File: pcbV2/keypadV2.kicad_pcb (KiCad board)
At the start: 2 copper layers, 93.7 x 93.3 mm, 59 parts, among them J1 Conn_01x02_Female, J2 USB_C_Receptacle, J3 Conn_01x03_Male, J6 Conn_01x03_Male, Q1 Q_NMOS_GSD, Q2 Q_NMOS_GSD, SW1 SW_Push, SW10 SW_Push, SW11 SW_Push, SW12 SW_Push, SW13 SW_SPDT, SW14 SW_Push, SW15 SW_Push, SW16 SW_Push, SW17 SW_DIP_x03, SW2 SW_Push, SW3 SW_Push, SW4 SW_Push, SW5 SW_Push, SW6 SW_Push, SW7 SW_Push, SW8 SW_Push, SW9 SW_Push, U1 Teensy4.0, U2 Waveshare_OLED_RGB

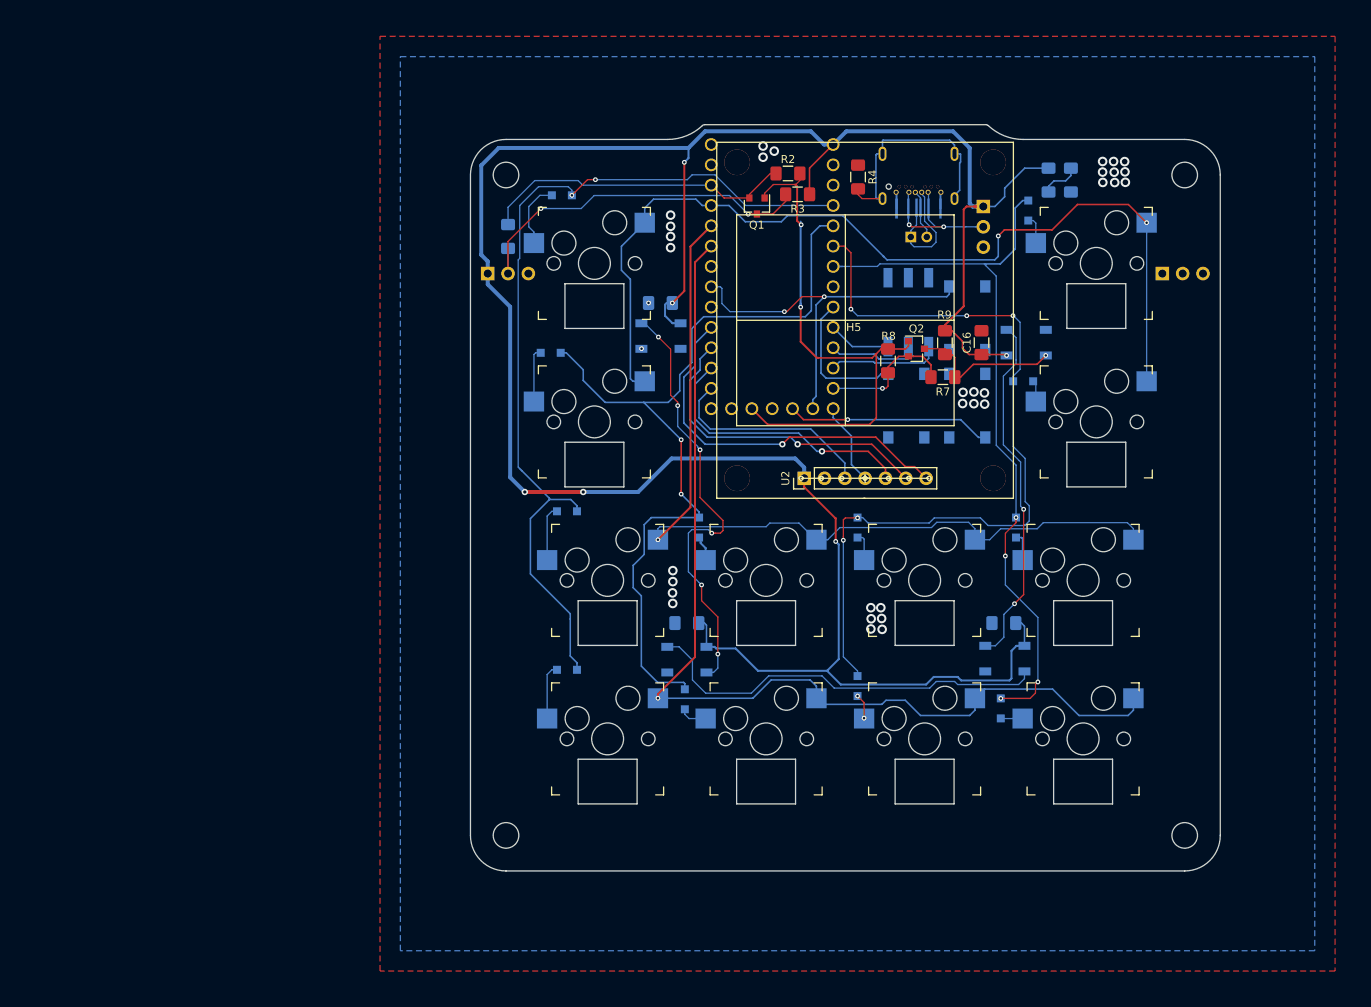
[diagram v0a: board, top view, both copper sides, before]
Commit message: removed usb c
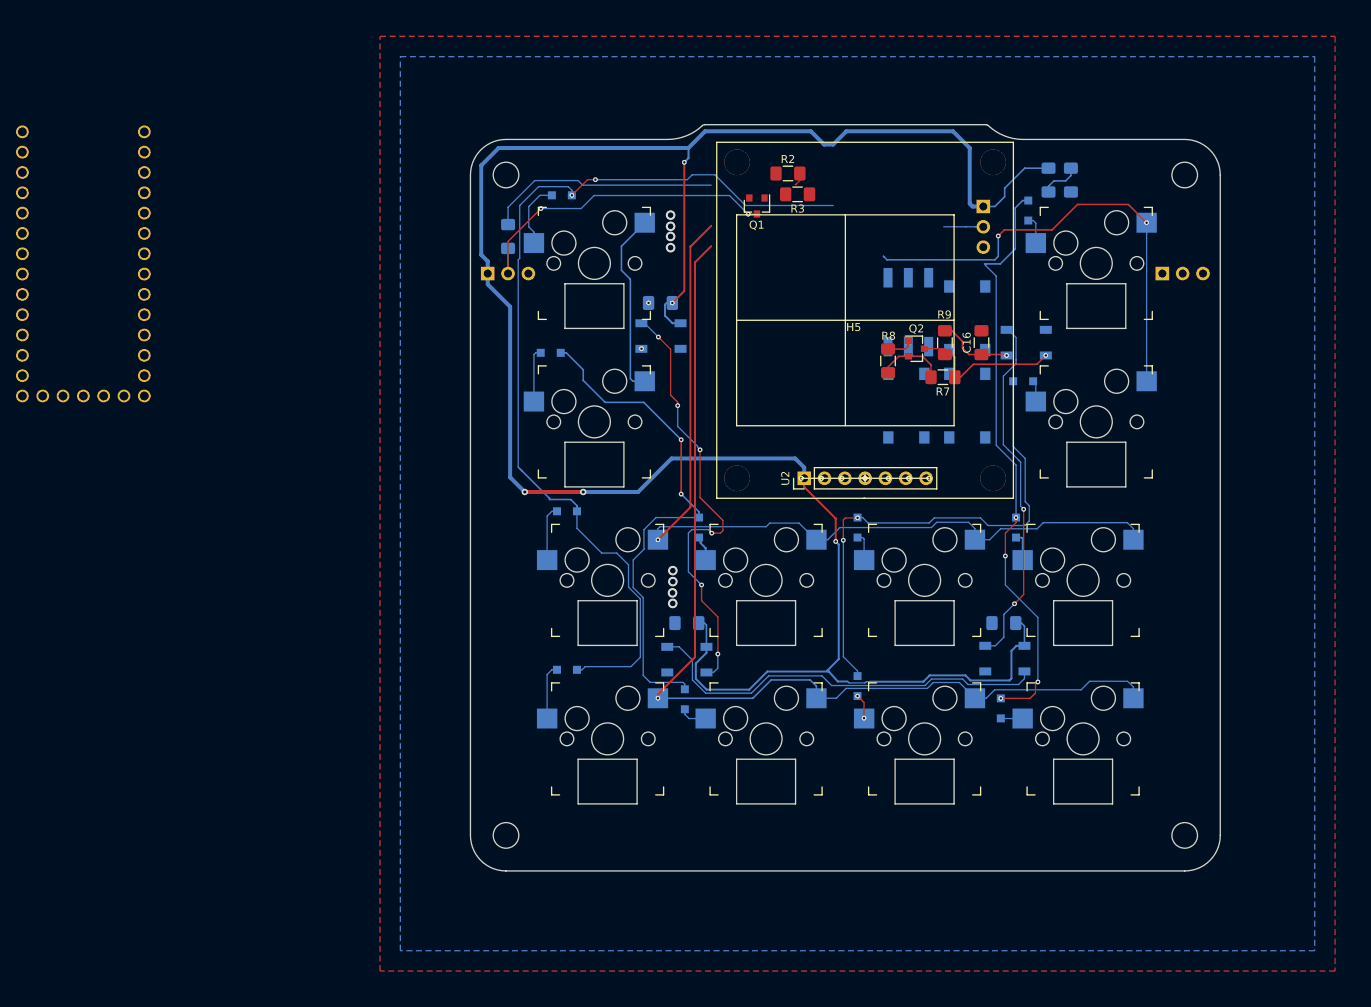
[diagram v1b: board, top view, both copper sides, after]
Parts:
- removed J1: Conn_01x02_Female, Connector_PinHeader_2.00mm:PinHeader_1x02_P2.00mm_Vertical
- removed J2: USB_C_Receptacle, custom:USB_C_REDUCED_UJ31-CH-G2
- removed R4: R_SHIELD, Resistor_SMD:R_1206_3216Metric_Pad1.42x1.75mm_HandSolder
- moved U1 86.1 mm to (86.6, 61.0)
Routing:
- net +3V3: track 67.6 -> 4.99 mm, vias 2 -> 0
- net ON_OFF: track 48.6 -> 0.00 mm, vias 2 -> 0
- net DISP_RST: track 47.3 -> 0.00 mm, vias 1 -> 0
- net COL2: track 106.0 -> 64.1 mm
- net DISP_DC: track 40.1 -> 0.00 mm, vias 1 -> 0
- net COL3: track 102.2 -> 63.1 mm, vias 5 -> 2
- net ROW1: track 117.1 -> 81.4 mm
- net CS: track 34.8 -> 0.00 mm, vias 1 -> 0
- net Net-(J2-PadS1): track 29.7 -> 0.00 mm
- net MOSI: track 26.8 -> 0.00 mm
- net PRGM: track 25.6 -> 0.00 mm, vias 1 -> 0
- net +5V: track 306.9 -> 287.0 mm
- net COL4: track 93.0 -> 74.0 mm
- net BTN: track 17.8 -> 0.00 mm
- net USB_DATA+: track 15.6 -> 0.00 mm
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
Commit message: started rewiring
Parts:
- removed SW13: SW_SPDT, Connector_PinHeader_2.54mm:PinHeader_1x03_P2.54mm_Vertical
- C16: moved to B.Cu
- moved U1 95.3 mm to (181.9, 62.7)
- moved SW14 29.3 mm to (168.1, 63.0), turned to 180 degrees
- moved SW15 29.2 mm to (168.1, 75.2)
- moved Q1 11.6 mm to (182.4, 53.6)
- moved SW17 10.0 mm to (197.4, 60.5)
- moved SW16 9.06 mm to (196.8, 73.4)
- moved R9 8.58 mm to (185.9, 69.0)
- moved C16 7.63 mm to (203.7, 64.9)
- moved R2 7.56 mm to (182.2, 49.4)
- moved Q2 5.26 mm to (185.9, 73.7), turned to 90 degrees
- moved R8 3.84 mm to (185.9, 76.7), turned to 0 degrees
- moved R7 2.73 mm to (196.7, 74.5)
- moved R3 2.48 mm to (178.2, 53.2), turned to 270 degrees
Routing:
- net COL4: track 74.0 -> 28.9 mm
- net COL2: track 64.1 -> 109.1 mm, vias 2 -> 0
- net ROW1: track 81.4 -> 41.4 mm, vias 2 -> 0
- net DISP_RST: track 0.00 -> 32.0 mm
- net COL3: track 63.1 -> 91.1 mm
- net DISP_DC: track 0.00 -> 26.7 mm
- net +5V: track 287.0 -> 261.6 mm
- net SCK: track 0.00 -> 22.2 mm
- net CS: track 0.00 -> 21.9 mm
- net RGB_DATA1: track 29.2 -> 49.2 mm
- net Net-(D26-Pad4): track 55.2 -> 36.1 mm, vias 6 -> 3
- net RGB_UNDER: track 19.6 -> 1.57 mm, vias 1 -> 0
- net DIP1: track 0.00 -> 17.6 mm
- net MOSI: track 0.00 -> 17.0 mm
- net DIP2: track 0.00 -> 12.9 mm
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- removed copper zone on B.Cu, net GND

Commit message: v2 layout
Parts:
- C16: moved to F.Cu
- moved C16 5.88 mm to (204.3, 70.7)
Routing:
- net ROW1: track 41.4 -> 112.0 mm
- net +5V: track 261.6 -> 322.4 mm, vias 6 -> 7
- net COL4: track 28.9 -> 71.9 mm, vias 4 -> 5
- net +3V3: track 3.36 -> 43.7 mm, vias 0 -> 2
- net ON_OFF: track 5.07 -> 34.4 mm, vias 0 -> 1
- net RGB_UNDER: track 1.57 -> 27.1 mm
- net COL2: track 109.1 -> 134.3 mm, vias 0 -> 2
- net PRGM: track 0.00 -> 15.8 mm, vias 0 -> 1
- net Net-(D26-Pad4): track 36.1 -> 48.9 mm, vias 3 -> 2
- net RGB_DATA2: track 0.00 -> 11.5 mm
- net BTN: track 0.00 -> 7.16 mm, vias 0 -> 1
- net ROW2: track 113.5 -> 120.2 mm
- net ROW3: track 137.7 -> 140.0 mm
- net COL1: track 128.8 -> 127.4 mm
- net RGB_DIN: track 54.2 -> 55.0 mm, vias 2 -> 3
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- added copper zone on B.Cu, net GND

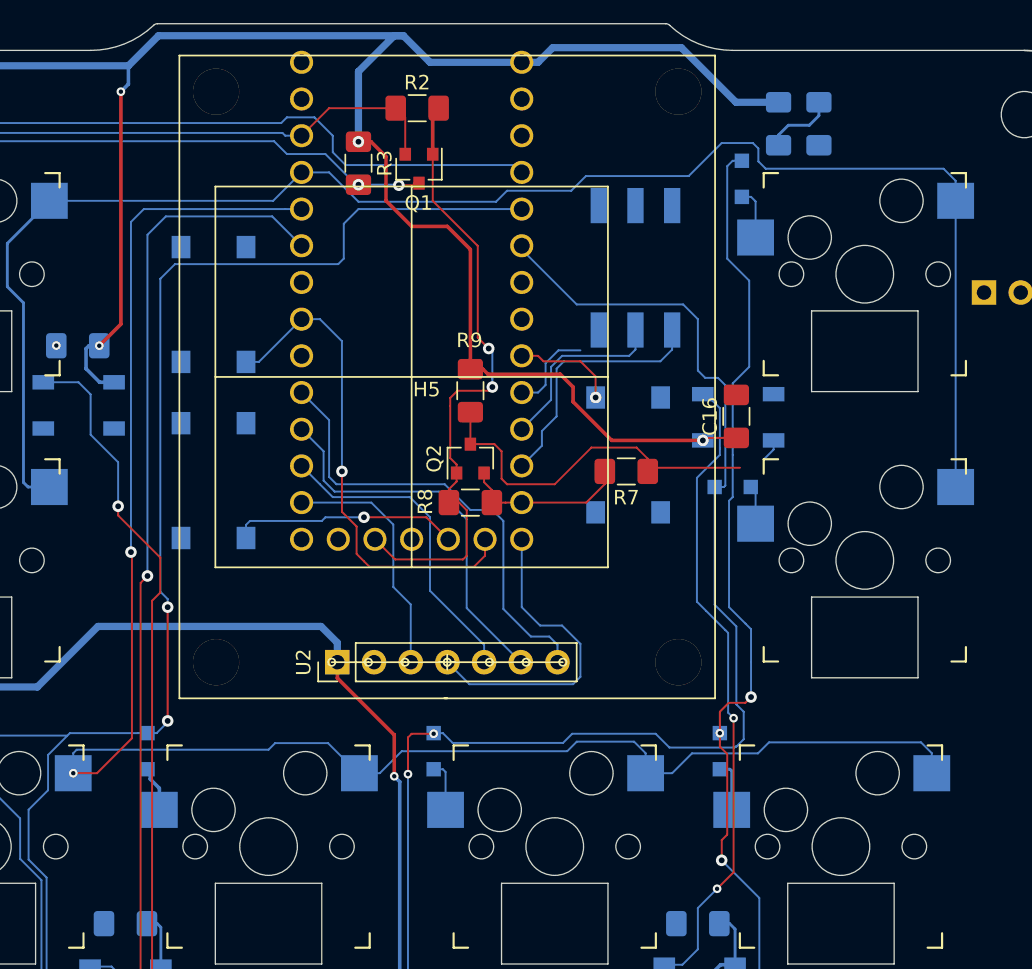
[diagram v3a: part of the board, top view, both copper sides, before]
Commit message: edited layout, updated daughter board
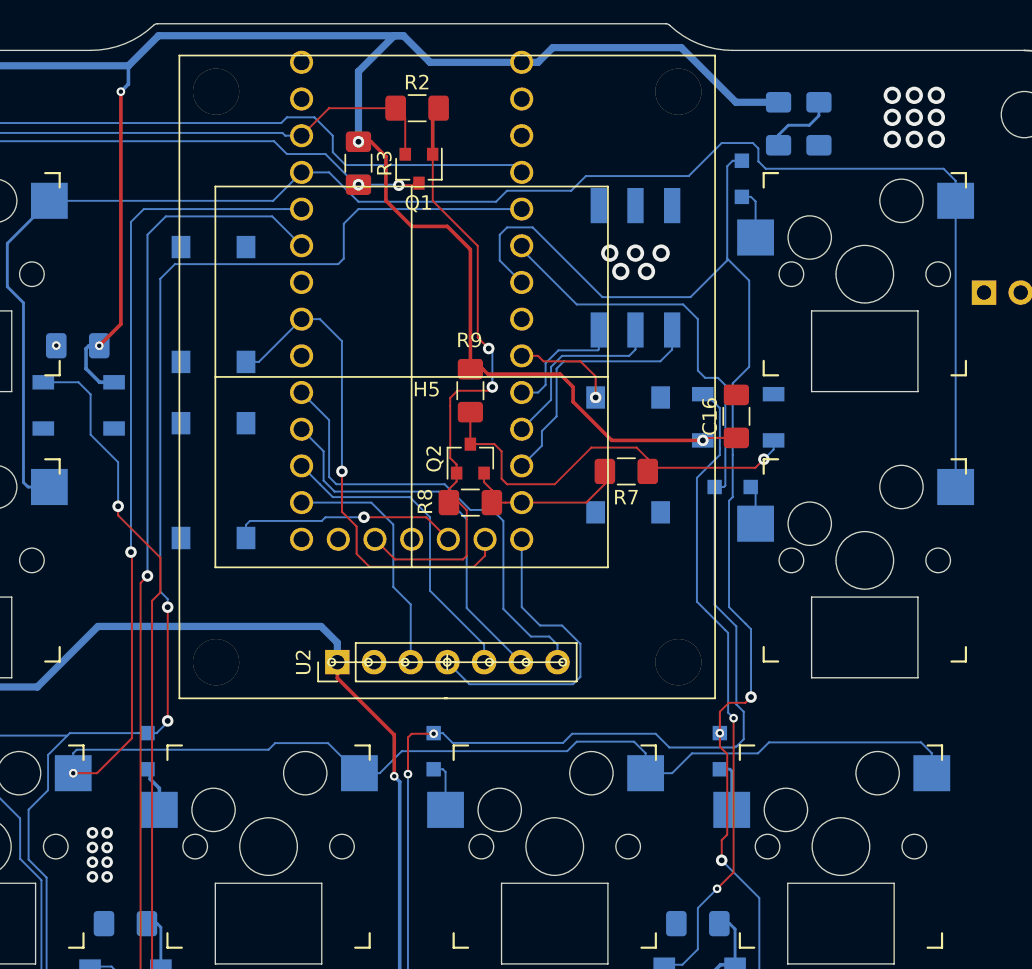
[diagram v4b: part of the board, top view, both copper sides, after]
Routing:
- net COL4: track 71.9 -> 95.0 mm
- net DIP3: track 6.16 -> 8.81 mm
- net RGB_UNDER: track 27.1 -> 29.0 mm, vias 0 -> 1
- net GND: vias 1 -> 23
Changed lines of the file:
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@@
     (thickness 1.6)
     (drawings 64)
-    (tracks 594)
+    (tracks 628)
     (zones 0)
     (modules 55)
@@
   (gr_arc (start 139.446 132.3975) (end 135.001 132.3975) (angle -90) (layer Edge.Cuts) (width 0.12))
   (via (at 157.2641 65.8368) (size 0.6) (drill 0.3) (layers F.Cu B.Cu) (net 1))
+  (via (at 215.138 48.514) (size 1.2) (drill 0.7) (layers F.Cu B.Cu) (net 1))
+  (via (at 216.662 48.514) (size 1.2) (drill 0.7) (layers F.Cu B.Cu) (net 1))
+  (via (at 215.138 50.038) (size 1.2) (drill 0.7) (layers F.Cu B.Cu) (net 1))
+  (via (at 216.662 50.038) (size 1.2) (drill 0.7) (layers F.Cu B.Cu) (net 1))
+  (via (at 218.186 50.038) (size 1.2) (drill 0.7) (layers F.Cu B.Cu) (net 1))
+  (via (at 218.186 48.514) (size 1.2) (drill 0.7) (layers F.Cu B.Cu) (net 1))
+  (via (at 218.186 51.562) (size 1.2) (drill 0.7) (layers F.Cu B.Cu) (net 1))
+  (via (at 216.662 51.562) (size 1.2) (drill 0.7) (layers F.Cu B.Cu) (net 1))
+  (via (at 215.138 51.562) (size 1.2) (drill 0.7) (layers F.Cu B.Cu) (net 1))
+  (via (at 195.58 59.436) (size 1.2) (drill 0.7) (layers F.Cu B.Cu) (net 1))
+  (via (at 197.358 59.436) (size 1.2) (drill 0.7) (layers F.Cu B.Cu) (net 1))
+  (via (at 199.136 59.436) (size 1.2) (drill 0.7) (layers F.Cu B.Cu) (net 1))
+  (via (at 198.12 60.706) (size 1.2) (drill 0.7) (layers F.Cu B.Cu) (net 1))
+  (via (at 196.342 60.706) (size 1.2) (drill 0.7) (layers F.Cu B.Cu) (net 1))
+  (via (at 160.782 100.584) (size 0.8) (drill 0.4) (layers F.Cu B.Cu) (net 1))
+  (via (at 160.782 101.6) (size 0.8) (drill 0.4) (layers F.Cu B.Cu) (net 1))
+  (via (at 160.782 102.616) (size 0.8) (drill 0.4) (layers F.Cu B.Cu) (net 1))
+  (via (at 159.766 102.616) (size 0.8) (drill 0.4) (layers F.Cu B.Cu) (net 1))
+  (via (at 159.766 101.6) (size 0.8) (drill 0.4) (layers F.Cu B.Cu) (net 1))
+  (via (at 159.766 100.584) (size 0.8) (drill 0.4) (layers F.Cu B.Cu) (net 1))
+  (via (at 160.782 99.568) (size 0.8) (drill 0.4) (layers F.Cu B.Cu) (net 1))
+  (via (at 159.766 99.568) (size 0.8) (drill 0.4) (layers F.Cu B.Cu) (net 1))
   (segment (start 162.2552 46.4693) (end 138.5316 46.4693) (width 0.5) (layer B.Cu) (net 2))
   (segment (start 138.5316 46.4693) (end 136.3472 48.6537) (width 0.5) (layer B.Cu) (net 2))
@@
   (segment (start 205.359 90.17) (end 205.359 90.17) (width 0.135) (layer B.Cu) (net 10))
   (via (at 205.359 90.17) (size 0.8) (drill 0.4) (layers F.Cu B.Cu) (net 10))
+  (segment (start 189.484 61.468) (end 187.96 59.944) (width 0.135) (layer B.Cu) (net 10))
+  (segment (start 187.96 59.944) (end 187.96 58.166) (width 0.135) (layer B.Cu) (net 10))
+  (segment (start 187.96 58.166) (end 188.468 57.658) (width 0.135) (layer B.Cu) (net 10))
+  (segment (start 188.468 57.658) (end 190.246 57.658) (width 0.135) (layer B.Cu) (net 10))
+  (segment (start 190.246 57.658) (end 195.072 62.484) (width 0.135) (layer B.Cu) (net 10))
+  (segment (start 195.072 62.484) (end 201.168 62.484) (width 0.135) (layer B.Cu) (net 10))
+  (segment (start 201.168 62.484) (end 203.708 59.944) (width 0.135) (layer B.Cu) (net 10))
+  (segment (start 203.708 59.944) (end 203.708 59.817) (width 0.135) (layer B.Cu) (net 10))
   (segment (start 145.181 91.8845) (end 145.816 91.8845) (width 0.135) (layer B.Cu) (net 11))
   (segment (start 144.586 92.4795) (end 145.181 91.8845) (width 0.135) (layer B.Cu) (net 11))
@@
   (segment (start 191.516 69.596) (end 189.484 71.628) (width 0.135) (layer B.Cu) (net 33))
   (segment (start 191.516 67.31) (end 191.516 69.596) (width 0.135) (layer B.Cu) (net 33))
-  (segment (start 190.61537 69.088) (end 191.135 68.56837) (width 0.135) (layer B.Cu) (net 34))
+  (segment (start 194.818 66.112) (end 194.818 64.757) (width 0.135) (layer B.Cu) (net 34))
   (segment (start 189.484 69.088) (end 190.61537 69.088) (width 0.135) (layer B.Cu) (net 34))
-  (segment (start 191.135 67.056) (end 192.024 66.167) (width 0.135) (layer B.Cu) (net 34))
+  (segment (start 192.024 66.167) (end 194.763 66.167) (width 0.135) (layer B.Cu) (net 34))
+  (segment (start 194.763 66.167) (end 194.818 66.112) (width 0.135) (layer B.Cu) (net 34))
+  (segment (start 190.61537 69.088) (end 191.135 68.56837) (width 0.135) (layer B.Cu) (net 34))
   (segment (start 191.135 68.56837) (end 191.135 67.056) (width 0.135) (layer B.Cu) (net 34))
-  (segment (start 192.024 66.167) (end 193.548 66.167) (width 0.135) (layer B.Cu) (net 34))
+  (segment (start 191.135 67.056) (end 192.024 66.167) (width 0.135) (layer B.Cu) (net 34))
   (segment (start 184.3405 87.757) (end 185.8645 89.281) (width 0.135) (layer B.Cu) (net 36))
   (segment (start 185.8645 89.281) (end 193.04 89.281) (width 0.135) (layer B.Cu) (net 36))
@@
   (segment (start 206.92 73.0375) (end 206.248 73.7095) (width 0.135) (layer B.Cu) (net 49))
   (segment (start 206.92 72.4025) (end 206.92 73.0375) (width 0.135) (layer B.Cu) (net 49))
-  (segment (start 198.4645 74.295) (end 198.2105 74.549) (width 0.135) (layer F.Cu) (net 49))
-  (segment (start 204.597 74.295) (end 198.4645 74.295) (width 0.135) (layer F.Cu) (net 49))
+  (segment (start 205.6625 74.295) (end 206.248 73.7095) (width 0.135) (layer F.Cu) (net 49))
+  (segment (start 198.4645 74.295) (end 205.6625 74.295) (width 0.135) (layer F.Cu) (net 49))
+  (segment (start 198.2105 74.549) (end 198.4645 74.295) (width 0.135) (layer F.Cu) (net 49))
+  (via (at 206.248 73.7095) (size 0.8) (drill 0.4) (layers F.Cu B.Cu) (net 49))
   (segment (start 176.149 49.403) (end 180.7575 49.403) (width 0.135) (layer F.Cu) (net 53))
   (segment (start 174.244 51.308) (end 176.149 49.403) (width 0.135) (layer F.Cu) (net 53))
